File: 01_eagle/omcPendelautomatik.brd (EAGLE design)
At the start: 44.5 x 69.8 mm, 71 parts, among them IC1 PIC12F675, IC2 7805, IC3 L5970D, K1 NA-5V, T1 BSS138, T2 BSS138, X1 RT034 Typ 086, X2 2X3

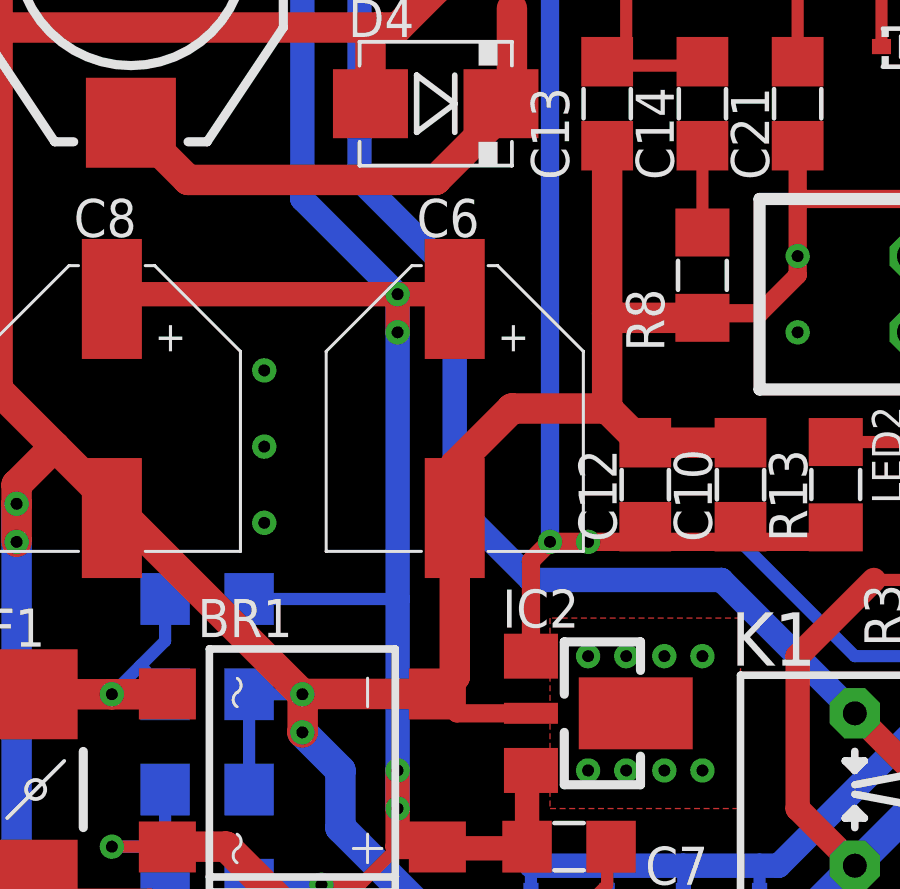
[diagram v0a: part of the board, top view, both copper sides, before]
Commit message: omcPendelautomatik.brd -> adjust cap to avoid DRC error
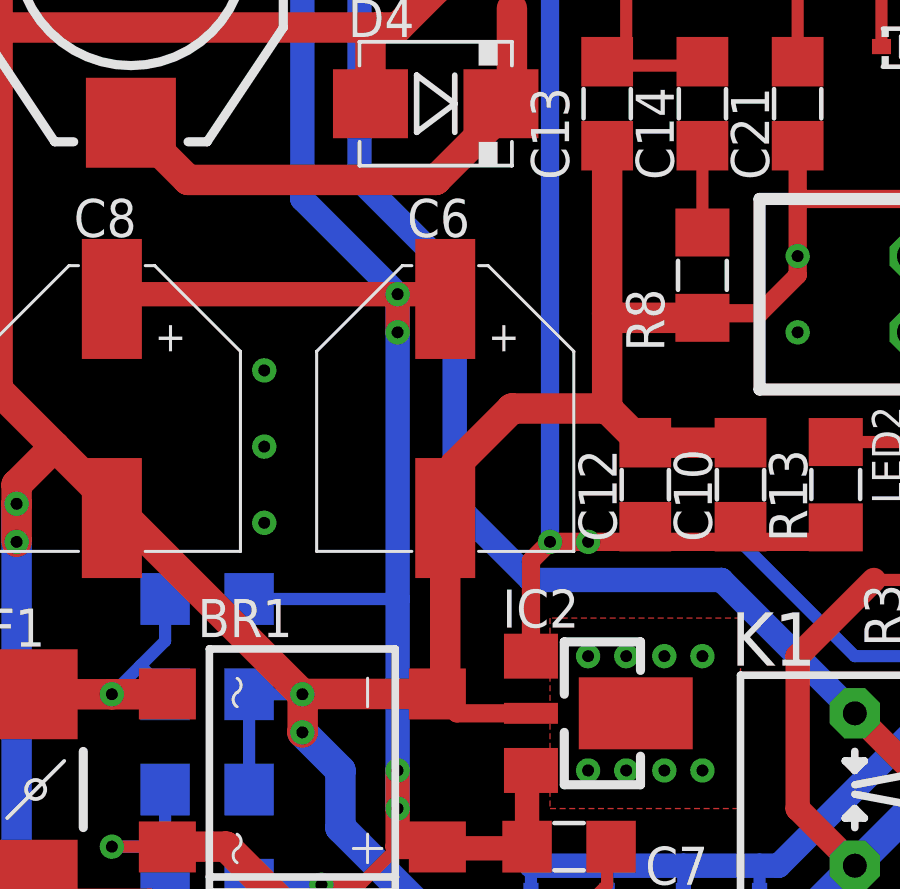
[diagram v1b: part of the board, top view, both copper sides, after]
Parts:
- moved C6 0.32 mm to (17.5, 27.9)
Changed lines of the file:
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@@
 <attribute name="NAME" x="11.7475" y="22.5425" size="1.27" layer="26" font="vector" rot="MR0"/>
 </element>
-<element name="C6" library="omcCapacitor" package="PANF" value="150µ/35V" x="17.78" y="27.94" smashed="yes">
-<attribute name="DIST#DIGIKEY#" value="" x="17.78" y="27.94" size="1.778" layer="27" display="off"/>
-<attribute name="DIST#REICHELT#" value="VF 150/35 P-F" x="17.78" y="27.94" size="1.778" layer="27" display="off"/>
-<attribute name="I_RIPPLE" value="850m" x="17.78" y="27.94" size="1.778" layer="27" display="off"/>
-<attribute name="VENDOR#" value="PANASONIC#EEEFP1V151AP" x="17.78" y="27.94" size="1.778" layer="27" display="off"/>
-<attribute name="DIST#CONRAD#" value="" x="17.78" y="27.94" size="1.778" layer="27" display="off"/>
-<attribute name="ESR" value="0R08" x="17.78" y="27.94" size="1.778" layer="27" display="off"/>
-<attribute name="NAME" x="16.51" y="33.655" size="1.27" layer="25" font="vector"/>
+<element name="C6" library="omcCapacitor" package="PANF" value="150µ/35V" x="17.4625" y="27.94" smashed="yes">
+<attribute name="DIST#DIGIKEY#" value="" x="17.4625" y="27.94" size="1.778" layer="27" display="off"/>
+<attribute name="DIST#REICHELT#" value="VF 150/35 P-F" x="17.4625" y="27.94" size="1.778" layer="27" display="off"/>
+<attribute name="I_RIPPLE" value="850m" x="17.4625" y="27.94" size="1.778" layer="27" display="off"/>
+<attribute name="VENDOR#" value="PANASONIC#EEEFP1V151AP" x="17.4625" y="27.94" size="1.778" layer="27" display="off"/>
+<attribute name="DIST#CONRAD#" value="" x="17.4625" y="27.94" size="1.778" layer="27" display="off"/>
+<attribute name="ESR" value="0R08" x="17.4625" y="27.94" size="1.778" layer="27" display="off"/>
+<attribute name="NAME" x="16.1925" y="33.655" size="1.27" layer="25" font="vector"/>
 </element>
 <element name="C7" library="omcCapacitor" package="1206" value="2µ2/50V" x="21.59" y="13.335" smashed="yes">
@@
 <wire x1="14.970125" y1="38.1" x2="14.970125" y2="40.370125" width="1.016" layer="1"/>
 <wire x1="14.970125" y1="40.370125" x2="15.24" y2="40.64" width="1.016" layer="1"/>
-<wire x1="17.78" y1="19.005" x2="17.2" y2="18.425" width="1.016" layer="1"/>
+<wire x1="17.4625" y1="19.005" x2="17.2" y2="18.425" width="1.016" layer="1"/>
 <via x="12.7" y="18.415" extent="1-16" drill="0.4" diameter="0.8128" shape="octagon"/>
 <via x="12.7" y="17.145" extent="1-16" drill="0.4" diameter="0.8128" shape="octagon"/>
@@
 <wire x1="6.35" y1="24.28875" x2="6.50875" y2="24.28875" width="1.016" layer="1"/>
 <wire x1="6.50875" y1="24.28875" x2="6.6675" y2="24.4475" width="1.016" layer="1"/>
-<wire x1="17.78" y1="19.005" x2="17.78" y2="24.28875" width="1.016" layer="1"/>
+<wire x1="17.4625" y1="19.005" x2="17.4625" y2="24.28875" width="1.016" layer="1"/>
 <wire x1="6.6675" y1="24.4475" x2="4.445" y2="26.67" width="1.016" layer="1"/>
 <wire x1="4.445" y1="26.67" x2="2.54" y2="28.575" width="1.016" layer="1"/>
@@
 <wire x1="20.955" y1="47.685" x2="20.955" y2="45.72" width="0.4064" layer="1"/>
 <wire x1="20.955" y1="45.72" x2="17.145" y2="45.72" width="0.8128" layer="1"/>
-<wire x1="17.93875" y1="24.13" x2="17.78" y2="24.28875" width="0.8128" layer="1"/>
+<wire x1="17.93875" y1="24.13" x2="17.4625" y2="24.28875" width="0.8128" layer="1"/>
 <wire x1="6.985" y1="3.175" x2="29.845" y2="3.175" width="1.016" layer="16"/>
 <wire x1="29.845" y1="3.175" x2="37.465" y2="3.175" width="1.016" layer="16"/>
@@
 <wire x1="8.89" y1="68.58" x2="35.56" y2="68.58" width="1.016" layer="16"/>
 <wire x1="35.56" y1="68.58" x2="39.37" y2="64.77" width="1.016" layer="16"/>
-<wire x1="17.78" y1="26.035" x2="17.78" y2="24.28875" width="1.016" layer="1"/>
+<wire x1="17.78" y1="26.035" x2="17.4625" y2="24.28875" width="1.016" layer="1"/>
 <wire x1="17.78" y1="26.035" x2="19.685" y2="27.94" width="1.016" layer="1"/>
 <wire x1="19.685" y1="27.94" x2="22.86" y2="27.94" width="1.016" layer="1"/>
@@
 <wire x1="15.875" y1="30.48" x2="15.875" y2="31.75" width="0.8128" layer="16"/>
 <wire x1="15.875" y1="31.75" x2="17.62125" y2="31.75" width="0.8128" layer="1"/>
-<wire x1="17.62125" y1="31.75" x2="17.78" y2="31.59125" width="0.8128" layer="1"/>
+<wire x1="17.62125" y1="31.75" x2="17.4625" y2="31.59125" width="0.8128" layer="1"/>
 <wire x1="15.875" y1="31.75" x2="6.50875" y2="31.75" width="0.8128" layer="1"/>
 <wire x1="6.50875" y1="31.75" x2="6.35" y2="31.59125" width="0.8128" layer="1"/>

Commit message: omcPendelautomatik -> added label with name and version
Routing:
- net GND: vias 66 -> 67
- added copper zone on layer 16, net N$31
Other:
- board text added: "OMC Adorf"
- board text added: "V1.0, 04/2019"
- board text added: "omcPendelautomatik"
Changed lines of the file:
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@@
 <text x="27.94" y="67.6275" size="1.4224" layer="1" font="vector" ratio="15">+TIV-</text>
 <text x="27.94" y="67.6275" size="1.4224" layer="25" font="vector" ratio="15">+TIV-</text>
+<text x="10.16" y="67.31" size="1.016" layer="16" font="vector" ratio="15" rot="MR180">omcPendelautomatik</text>
+<text x="10.16" y="66.04" size="1.016" layer="16" font="vector" ratio="15" rot="MR180">OMC Adorf</text>
+<text x="10.16" y="64.77" size="1.016" layer="16" font="vector" ratio="15" rot="MR180">V1.0, 04/2019</text>
 </plain>
 <attributes>
@@
 <wire x1="17.78" y1="52.07" x2="16.51" y2="52.07" width="0.4064" layer="16"/>
 <wire x1="17.65" y1="51.94" x2="17.78" y2="52.07" width="0.4064" layer="16"/>
-<wire x1="29.21" y1="60.96" x2="20.47875" y2="60.96" width="0.6096" layer="1"/>
+<wire x1="29.21" y1="60.96" x2="22.225" y2="60.96" width="0.6096" layer="1"/>
+<wire x1="22.225" y1="60.96" x2="20.47875" y2="60.96" width="0.6096" layer="1"/>
 <wire x1="20.32" y1="62.23" x2="20.47875" y2="62.38875" width="0.6096" layer="1"/>
 <contactref element="C21" pad="1"/>
@@
 <vertex x="27.305" y="20.955"/>
 </polygon>
+<via x="22.225" y="60.96" extent="1-16" drill="0.4" diameter="0.8128" shape="octagon"/>
 </signal>
 <signal name="VOUT">
@@
 </polygon>
 </signal>
+<signal name="N$31">
+<polygon width="0.4064" layer="16" pour="cutout">
+<vertex x="10.16" y="67.31"/>
+<vertex x="10.16" y="63.5"/>
+<vertex x="21.59" y="63.5"/>
+<vertex x="21.59" y="66.04"/>
+<vertex x="26.035" y="66.04"/>
+<vertex x="26.035" y="67.31"/>
+</polygon>
+</signal>
